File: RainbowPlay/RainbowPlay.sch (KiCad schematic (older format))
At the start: 47 parts, among them J1 GPIO_CONNECTOR, J2 PJ-102A, U1 LM386, U2 LM386

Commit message: Initial development in progress
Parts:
- removed C1, C2: 10uF, Capacitor_THT:C_Disc_D3.4mm_W2.1mm_P2.50mm, symbol RainbowPlay-rescue:C-Device
- removed C3, C4: 0.1uF, Capacitor_THT:C_Disc_D3.4mm_W2.1mm_P2.50mm, symbol RainbowPlay-rescue:C-Device
- removed C5, C6: 0.05uF, Capacitor_THT:C_Disc_D3.4mm_W2.1mm_P2.50mm, symbol RainbowPlay-rescue:C-Device
- removed C7, C8: 250uF, Capacitor_THT:CP_Radial_D8.0mm_P5.00mm, symbol RainbowPlay-rescue:CP1-Device
- removed J2: PJ-102A, digikey-footprints:Barrel_Jack_5.5mmODx2.1mmID_PJ-102A, symbol dk_Barrel-Power-Connectors:PJ-102A
- removed LS1, LS2: Speaker, Connector_PinHeader_2.54mm:PinHeader_2x01_P2.54mm_Vertical, symbol RainbowPlay-rescue:Speaker-Device
- removed MOD1: RN52-I_RM, kicad-footprints:rn52-breakout, symbol RainbowPlay-rescue:RN52-I_RM-dk_RF-Transceiver-Modules
- removed R1, R2: 1.2k, Resistor_THT:R_Axial_DIN0204_L3.6mm_D1.6mm_P5.08mm_Horizontal, symbol RainbowPlay-rescue:R-Device
- removed R3, R4: 10R, Resistor_THT:R_Axial_DIN0204_L3.6mm_D1.6mm_P5.08mm_Horizontal, symbol RainbowPlay-rescue:R-Device
- removed S1, S10, S11, S2, S3, S4, S5, S6, S7, S8, S9: 1825910-6, digikey-footprints:Switch_Tactile_THT_6x6mm, symbol dk_Tactile-Switches:1825910-6
- removed U1, U2: LM386, Package_DIP:DIP-8_W7.62mm_Socket, symbol RainbowPlay-rescue:LM386-Amplifier_Audio
- added C10: 220pF, symbol Device:C
- added C14: 1uF, symbol Device:C
- added C15, C16: 10uF, symbol Device:C
- added C3: 1.5uF, Capacitor_SMD:C_0603_1608Metric, symbol Device:C
- added C4, C5: 0.1uF, Capacitor_SMD:C_0603_1608Metric, symbol Device:C
- added C8, C9: 0.1uF, symbol Device:C
- added D1, D10, D11, D12, D2, D3, D4, D5, D6, D7, D8, D9: SK6812, LED_SMD:LED_SK6812_PLCC4_5.0x5.0mm_P3.2mm, symbol LED:SK6812
- added D13: LED, symbol Device:LED
- added J2: Conn_01x06_Male, symbol Connector:Conn_01x06_Male
- added J3: Conn_01x04_Male, Connector_PinHeader_2.54mm:PinHeader_1x04_P2.54mm_Vertical, symbol Connector:Conn_01x04_Male
- added LS1, LS2: Speaker, Connector_PinHeader_2.54mm:PinHeader_1x02_P2.54mm_Vertical, symbol Device:Speaker
- added Q1, Q2: BSS138, digikey-footprints:SOT-23-3, symbol dk_Transistors-FETs-MOSFETs-Single:BSS138
- added R3, R4: 5R, Resistor_SMD:R_0603_1608Metric, symbol Device:R
- added R5, R6: 10k, Resistor_SMD:R_0603_1608Metric, symbol Device:R
- added S1: AB11AH-FA, digikey-footprints:PushButton_12x12mm_THT_GPTS203211B, symbol RainbowPlay:AB11AH-FA
- added SWA1, SWB1, SWC1, SWD1, SWE1: B3F-3152, B3F3152, symbol B3F-3152:B3F-3152
- added U1: TPA2001D2, Package_SO:HTSSOP-24-1EP_4.4x7.8mm_P0.65mm_EP3.2x5mm, symbol RainbowPlay:TPA2001D2
- C1: renamed from C9; footprint (none) -> Capacitor_SMD:C_0603_1608Metric
- C11: value 1uF -> 0.1uF
- C12, C13: value 47nF -> 0.1uF
- C2: renamed from C10; footprint (none) -> Capacitor_SMD:C_0603_1608Metric
- C6: renamed from C14; value 47nF -> 0.1uF; footprint (none) -> Capacitor_SMD:C_0603_1608Metric
- C7: renamed from C15; value 47nF -> 0.1uF; footprint (none) -> Capacitor_SMD:C_0603_1608Metric
- L1, L2: footprint (none) -> Inductor_SMD:L_0603_1608Metric; Part number (none) -> ASMCI-0603-100M-T; Price (none) -> $0.22; Vendor (none) -> Digikey
- R1: renamed from R5; footprint (none) -> Resistor_SMD:R_0603_1608Metric
- R2: renamed from R6; footprint (none) -> Resistor_SMD:R_0603_1608Metric
- R7: value 2.2k -> 120k; footprint (none) -> Resistor_SMD:R_0603_1608Metric
- R8: value 2.2k -> 200R; footprint (none) -> Resistor_SMD:R_0603_1608Metric
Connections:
- net labels added: AUD_L+, AUD_L-, AUD_R+, AUD_R-, EN, GAIN_0, GAIN_1, LB, LED, PWR_BTN, PWR_LED, UART_RX, UART_TX
- net labels removed: MIC_BIAS, MIC_L+, MIC_L-, MIC_R+, MIC_R-, NXT_TRK, PLY_PS, PREV_TRK, RXD0, SPI_CE1, SPI_MISO, SPI_MOSI, SPI_SCLK, TXD0, VOL_DWN, VOL_UP
- wire segments 165 -> 279
- no-connect marks 70 -> 25
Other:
- note added: "Audio amplifier (Class D stereo)"
- note added: "Filtering for PWM audio\ninto amp input"
- note added: "LEDs"
- note added: "Level-shift"
- note added: "PWR BTN"
- note added: "PWR LED"
- note added: "UART"
- note added: "UI buttons"
- note removed: "Audio amplifiers"
- note removed: "Bluetooth audio module"
- note removed: "Factory reset"
- note removed: "Filtering for PWM audio\ninto MIC input"
- note removed: "Optional gain"
- note removed: "User interface buttons"
- moved on the sheet: C1, C2, C6, C7, H1, H2, H3, H4, L2, R1, R2

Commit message: Development
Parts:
- S1: footprint digikey-footprints:PushButton_12x12mm_THT_GPTS203211B -> magic-music-box:AB11AH-FA
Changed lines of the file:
@@
 F 0 "S1" H 14425 6325 50  0000 C CNN
 F 1 "AB11AH-FA" H 14425 6234 50  0000 C CNN
-F 2 "digikey-footprints:PushButton_12x12mm_THT_GPTS203211B" H 14625 6250 50  0001 L CNN
+F 2 "magic-music-box:AB11AH-FA" H 14625 6250 50  0001 L CNN
 F 3 "http://switches-connectors-custom.cwind.com/Asset/GPTS203211BR2.pdf" H 14625 6350 60  0001 L CNN
 F 4 "CW181-ND" H 14625 6450 60  0001 L CNN "Digi-Key_PN"

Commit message: Development
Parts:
- removed C2: 1.5uF, Capacitor_SMD:C_0603_1608Metric, symbol Device:C
- removed Q2: BSS138, digikey-footprints:SOT-23-3, symbol dk_Transistors-FETs-MOSFETs-Single:BSS138
- removed R3, R4: 5R, Resistor_SMD:R_0603_1608Metric, symbol Device:R
- removed S1: AB11AH-FA, magic-music-box:AB11AH-FA, symbol RainbowPlay:AB11AH-FA
- added D? (x2): 1N5819HW-7-F, digikey-footprints:SOD-123, symbol dk_Diodes-Rectifiers-Single:1N5819HW-7-F
- added D?: LED, LED_SMD:LED_0603_1608Metric, symbol Device:LED
- added J? (x2): Conn_01x02_Male, symbol Connector:Conn_01x02_Male
- added Q? (x3): BSS138, digikey-footprints:SOT-23-3, symbol dk_Transistors-FETs-MOSFETs-Single:BSS138
- added R? (x4): 10k, Resistor_SMD:R_0603_1608Metric, symbol Device:R
- added R?: 200R, Resistor_SMD:R_0603_1608Metric, symbol Device:R
- added R?: 200k, Resistor_SMD:R_0603_1608Metric, symbol Device:R
- added SW?: SW_SPST, symbol Switch:SW_SPST
- added U?: SN74LVC1G32DBVRG4, symbol dk_Logic-Gates-and-Inverters:SN74LVC1G32DBVRG4
- C10, C11, C12, C13, C14, C15, C16, C8, C9: footprint (none) -> Capacitor_SMD:C_0603_1608Metric
- C4, C5, C6, C7: value 0.1uF -> 10uF
- D13: footprint (none) -> LED_SMD:LED_0603_1608Metric
- J2: footprint (none) -> Connector_PinHeader_2.54mm:PinHeader_1x06_P2.54mm_Vertical
- SWA1, SWB1, SWC1, SWD1, SWE1: footprint B3F3152 -> B3F-3152:B3F3152
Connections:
- net +3V3: now also Q?.1 (G)
- net +5V: now also D?.K, D?.K, J?.1 (Pin_1), J?.1 (Pin_1)
- net GND: now also J2.4 (Pin_4), Q?.2 (S), Q?.2 (S), R?.1, R?.1, R?.1, R?.1, SW?.1 (A), U?.3 (GND); no longer C9.2, J2.2 (Pin_2), U1.6 (AGND)
- net GNDA: now also C9.2, U1.6 (AGND)
- net LB: no longer J1.38 (Pin_38)
- net M1: now reaches J1.28 (Pin_28)
- net M1: now also Q?.1 (G), R?.2
- net Vs: now reaches J2.6 (Pin_6)
- net Vs: now also R?.2, R?.2, U?.5 (Vcc)
- net at D13.1 (K): now also R8.2
- net EN renamed PWR_EN
- net PWR_EN: now also U?.4 (Y)
- net PWR_BTN renamed PWR_OFF_BTN
- net PWR_LED renamed M2
- net M2: now also Q?.1 (G), R?.2
- new net: D?.A, J?.2 (Pin_2), Q?.3 (D) (x2)
- new net: D?.1 (K), R?.2
- new net: R?.1, SW?.2 (B), U?.2 (B)
- new net: Q?.3 (D), R?.1, U?.1 (A)
- new net AWAKE_SIG: D?.2 (A), J1.38 (Pin_38), Q?.2 (S), R?.2
- no-connect marks 25 -> 23
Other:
- note added: "4.2-5V"
- note added: "5V"
- note added: "Don’t turn me off! LED"
- note added: "Driven high by software,\nfloating when off"
- note added: "Misc drivers"
- note added: "PWR_EN only low when RPi is off and user switches OFF"
- note added: "Power up / Power down"
- note added: "SPI1 MISO"
- note removed: "PWR BTN"
- moved on the sheet: C1, C10, C11, C12, C13, C14, C15, C16, C3, C4, C5, C6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

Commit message: Development
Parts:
- removed SWA1, SWB1, SWC1, SWD1, SWE1: B3F-3152, B3F-3152:B3F3152, symbol B3F-3152:B3F-3152
- added H5, H6: MountingHole, lib:MountingHole_2.7mm_M2.5_uHAT_RPi, symbol RainbowPlay-rescue:MountingHole-Mechanical
- added J6: Conn_02x12_Odd_Even, Connector_PinSocket_2.54mm:PinSocket_2x12_P2.54mm_Vertical_SMD, symbol Connector_Generic:Conn_02x12_Odd_Even
- added S1, S2, S3, S4, S5: B3F-4050, B3F-4050:SW_B3F-4050, symbol B3F-4050:B3F-4050
- J1: footprint lib:PinSocket_2x20_P2.54mm_Vertical_Centered_Anchor -> Connector_PinSocket_2.54mm:PinSocket_2x20_P2.54mm_Vertical_SMD
- J4, J5: renamed from J?; footprint (none) -> Connector_PinHeader_2.54mm:PinHeader_1x02_P2.54mm_Vertical
- SW1: renamed from SW?; footprint (none) -> Button_Switch_THT:SW_PUSH_6mm
- U2: renamed from U?; footprint (none) -> Package_TO_SOT_SMD:SOT-23-5
- gave numbers to parts that had none: 12
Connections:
- net +3V3: now also J6.1 (Pin_1)
- net +5V: now also J6.2 (Pin_2), J6.4 (Pin_4)
- net BTN_A: now also S1.1, S1.2
- net BTN_B: now also S2.1, S2.2
- net BTN_C: now also S3.1, S3.2
- net BTN_D: now also S4.1, S4.2
- net BTN_E: now also S5.1, S5.2
- net GND: now also J6.14 (Pin_14), J6.20 (Pin_20), J6.6 (Pin_6), S1.3, S1.4, S2.3, S2.4, S3.3, S3.4, S4.3, S4.4, S5.3, S5.4
- net LED: now also J6.12 (Pin_12)
- net UART_RX: now also J6.10 (Pin_10)
- net UART_TX: now also J6.8 (Pin_8)
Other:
- note added: "(TFT) MOSI"
- note added: "(TFT) SCLK"
- note added: "(TFT) SPI1 MISO"
- note added: "(TFT) SPI_CE0"
- note added: "Adafruit MiniPi-TFT 1.3”"
- note added: "Aux drivers"
- note added: "Awake LED"
- note added: "GPIO 17"
- note added: "GPIO 22"
- note added: "GPIO 27"
- note added: "I2C1 SCL"
- note added: "I2C1 SDA"
- note added: "Mini-TFT"
- note removed: "Don’t turn me off! LED"
- note removed: "Misc drivers"
- note removed: "SPI1 MISO"
- note removed: "inky Busy"
- note removed: "inky Data/Command"
- note removed: "inky I2C1 SCL"
- note removed: "inky I2C1 SDA"
- note removed: "inky MOSI"
- note removed: "inky Reset"
- note removed: "inky SCLK"
- note removed: "inky SPI_CE0"
- moved on the sheet: C1, C10, C11, C12, C13, C14, C15, C16, C3, C4, C5, C6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

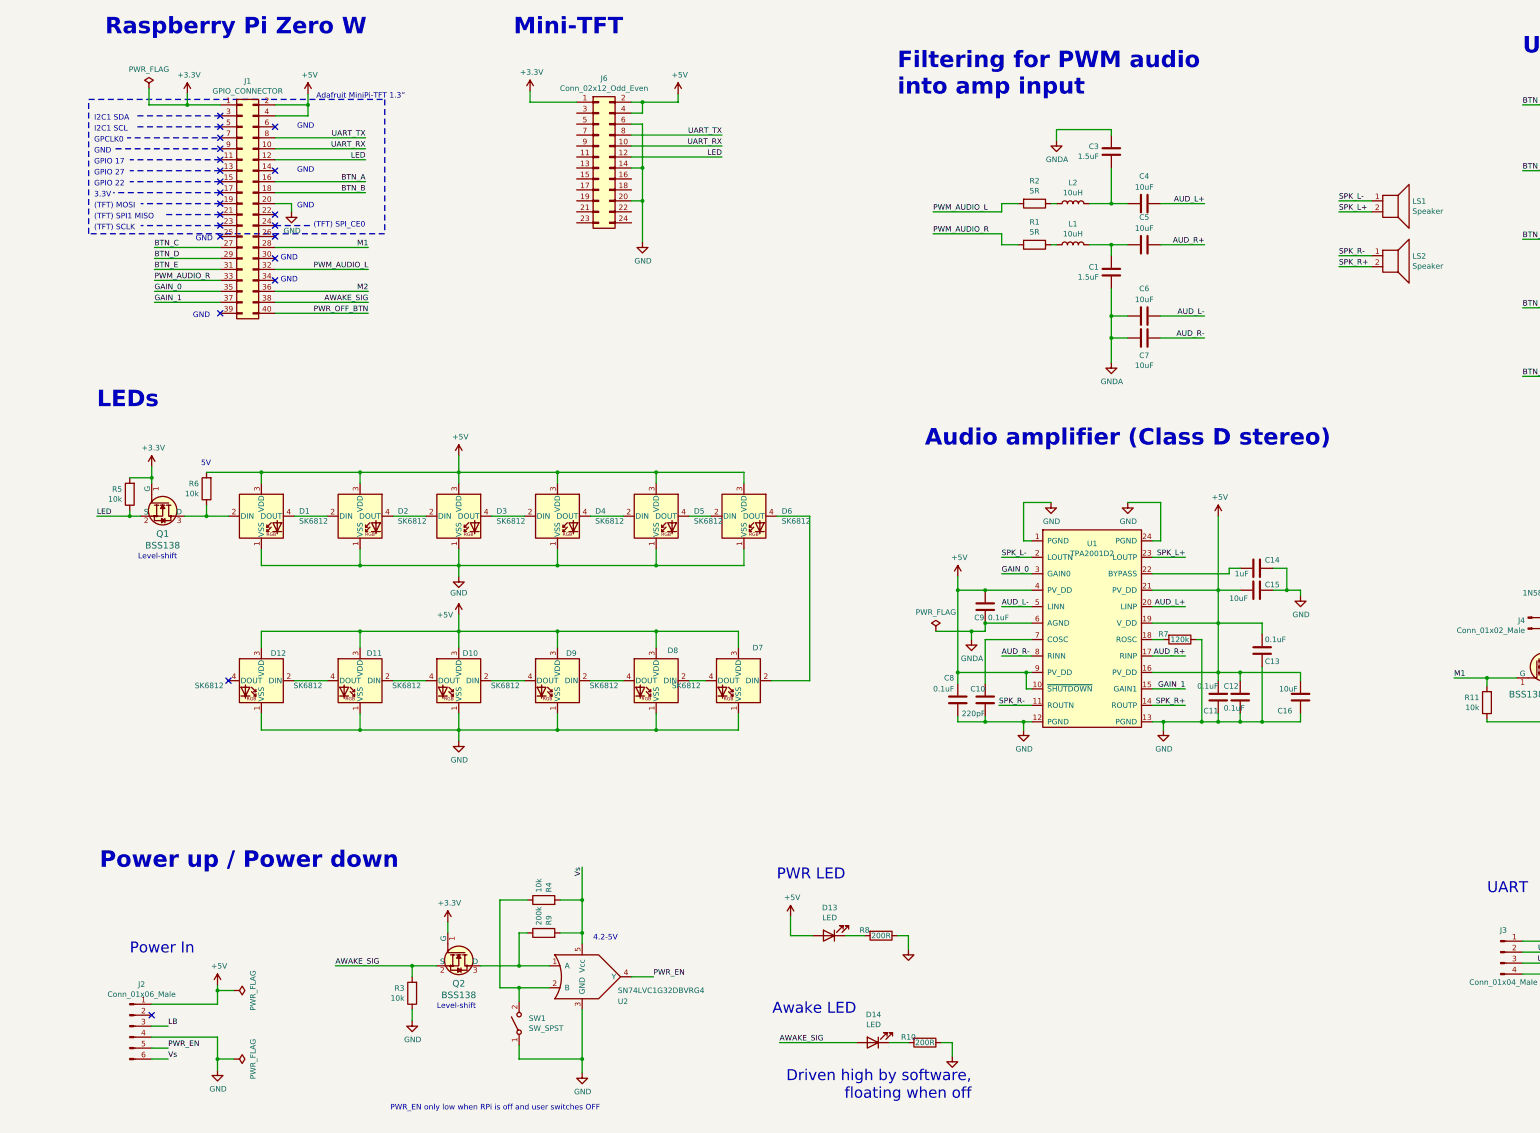
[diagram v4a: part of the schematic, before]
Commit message: PCB dev
- Work on power up, power down
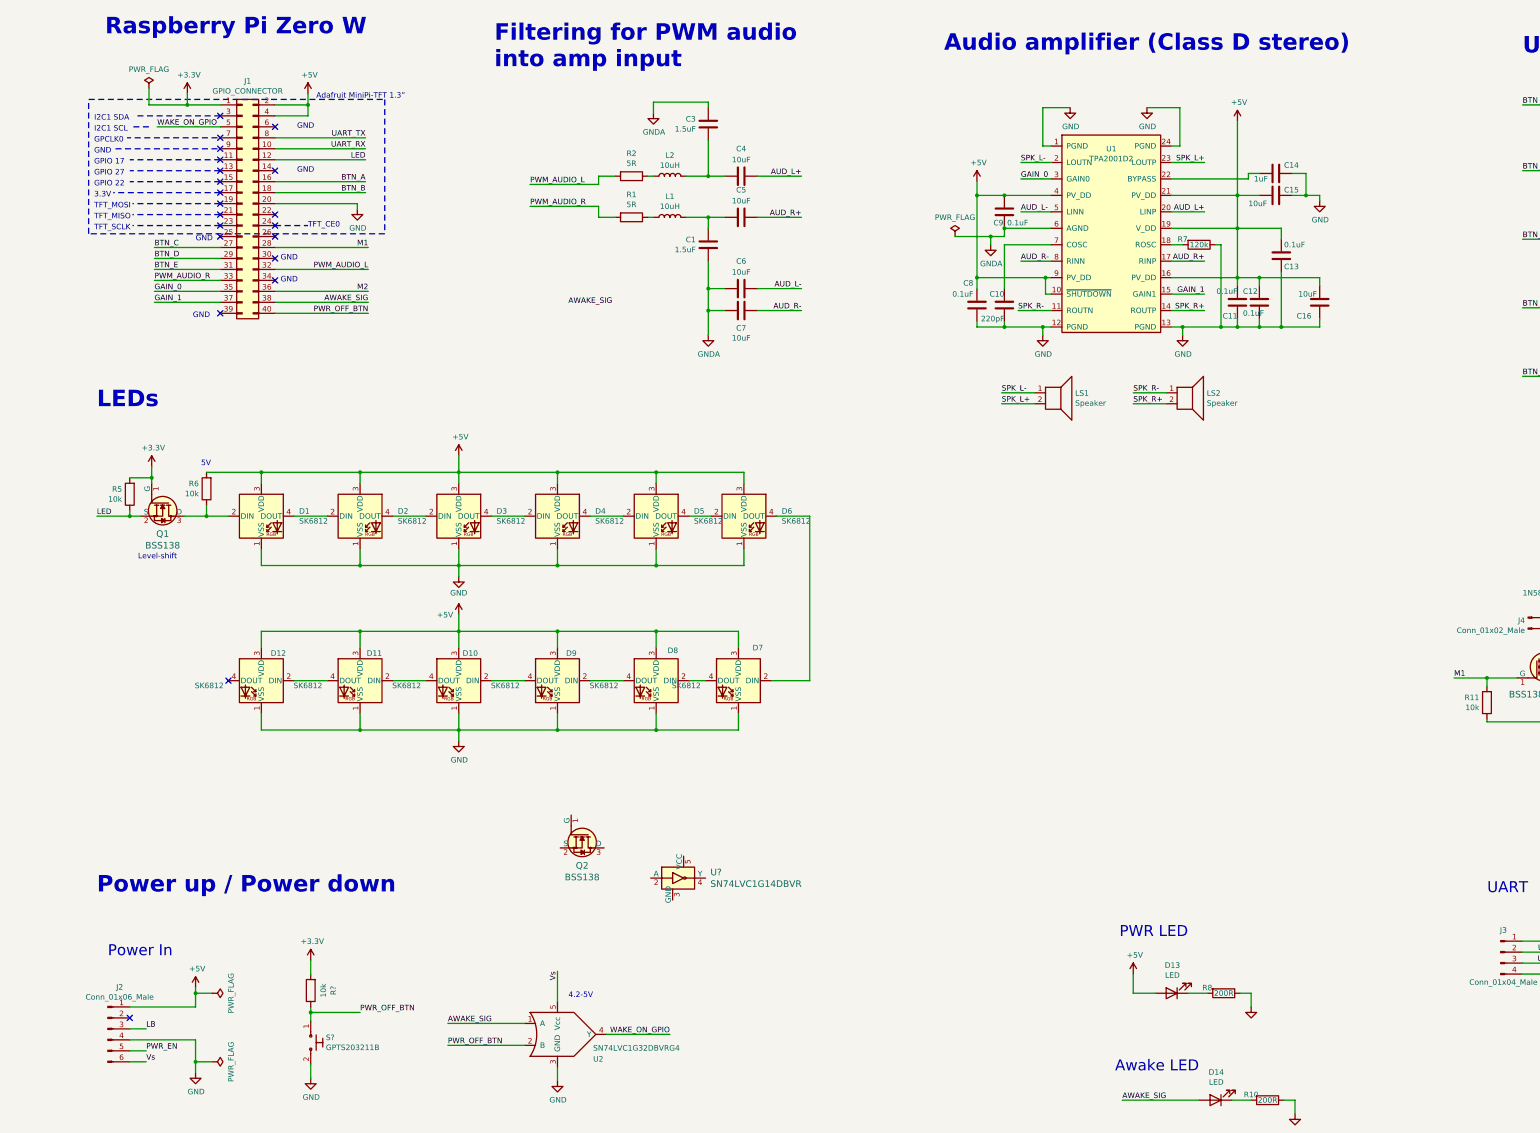
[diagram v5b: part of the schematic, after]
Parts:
- removed J6: Conn_02x12_Odd_Even, Connector_PinSocket_2.54mm:PinSocket_2x12_P2.54mm_Vertical_SMD, symbol Connector_Generic:Conn_02x12_Odd_Even
- removed R3, R4: 10k, Resistor_SMD:R_0603_1608Metric, symbol Device:R
- removed R9: 200k, Resistor_SMD:R_0603_1608Metric, symbol Device:R
- removed SW1: SW_SPST, Button_Switch_THT:SW_PUSH_6mm, symbol Switch:SW_SPST
- added R?: 10k, Resistor_SMD:R_0603_1608Metric, symbol Device:R
- added S?: GPTS203211B, digikey-footprints:PushButton_12x12mm_THT_GPTS203211B, symbol dk_Pushbutton-Switches:GPTS203211B
- added U?: SN74LVC1G14DBVR, digikey-footprints:SOT-753, symbol dk_Logic-Gates-and-Inverters:SN74LVC1G14DBVR
- J1: footprint Connector_PinSocket_2.54mm:PinSocket_2x20_P2.54mm_Vertical_SMD -> Connector_PinSocket_2.54mm:PinSocket_2x20_P2.54mm_Vertical
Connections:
- net +3V3: now also R?.2; no longer Q2.1 (G)
- net AWAKE_SIG: now also U2.1 (A); no longer Q2.2 (S)
- net GND: now also S?.2
- net PWR_EN: no longer U2.4 (Y)
- net PWR_OFF_BTN: now also U2.2 (B), R?.1, S?.1
- net WAKE_ON_GPIO: now reaches J1.5 (Pin_5)
- net WAKE_ON_GPIO: now also U2.4 (Y)
- net at Q2.3 (D): no longer U2.1 (A)
- no-connect marks 23 -> 22
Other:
- note added: "TFT_CE0"
- note added: "TFT_MISO"
- note added: "TFT_MOSI"
- note added: "TFT_SCLK"
- note removed: "(TFT) MOSI"
- note removed: "(TFT) SCLK"
- note removed: "(TFT) SPI1 MISO"
- note removed: "(TFT) SPI_CE0"
- note removed: "Driven high by software,\nfloating when off"
- note removed: "Mini-TFT"
- note removed: "PWR_EN only low when RPi is off and user switches OFF"
- moved on the sheet: C1, C10, C11, C12, C13, C14, C15, C16, C3, C4, C5, C6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
